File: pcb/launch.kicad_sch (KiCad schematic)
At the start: 250 parts, among them J1 Conn_ARM_SWD_TagConnect_TC2030, J6 SWD_TH, J7 AFC07-S20FCC-00, SW1 SKRPACE010, SW2 SKRPACE010, U1 RP2040, U24 W25Q16JVSSIQ, Y2 RH100-12.000-18-2030-TR

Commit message: hub reset handled by DC-DC power good switch to TLV62585P DC-DC for power good remove reset button - can just plug cable add buttons to ground SDA, SCL as hub bypass to allow programming
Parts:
- removed R35: 5.1 k, kicad_pcb:R_0402_1005Metric, symbol Device:R
- removed SW1: SKRPACE010, kicad_pcb:SW_SPST_PTS810, symbol Switch:SW_Push
- removed TP1, TP2: DNP, TestPoint:TestPoint_Loop_D1.80mm_Drill1.0mm_Beaded, symbol Connector:TestPoint
- added SW3, SW4: SKRPACE010, kicad_pcb:SW_SPST_PTS810, symbol Switch:SW_Push
- added TP1: Conn_01x03, Connector_PinHeader_2.54mm:PinHeader_1x03_P2.54mm_Vertical, symbol Connector_Generic:Conn_01x03
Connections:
- net RUN is gone; now on net +3V3: U1.26 (RUN)
- net GND: now also SW3.1, SW4.1, TP1.3 (Pin_3)
- net UC_SCL: now also SW4.2, TP1.1 (Pin_1)
- net UC_SDA: now also SW3.2, TP1.2 (Pin_2)
- net ~{RESET_USB}: no longer U1.31 (GPIO20)
- no-connect marks 3 -> 4
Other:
- sheet power ports: added PG; removed none
- note added: "hold SW3, SW4 while connecting power to use default USB hub configuration. This can be used to flash a blank or bricked board by USB DFU"
- note removed: "Reset"

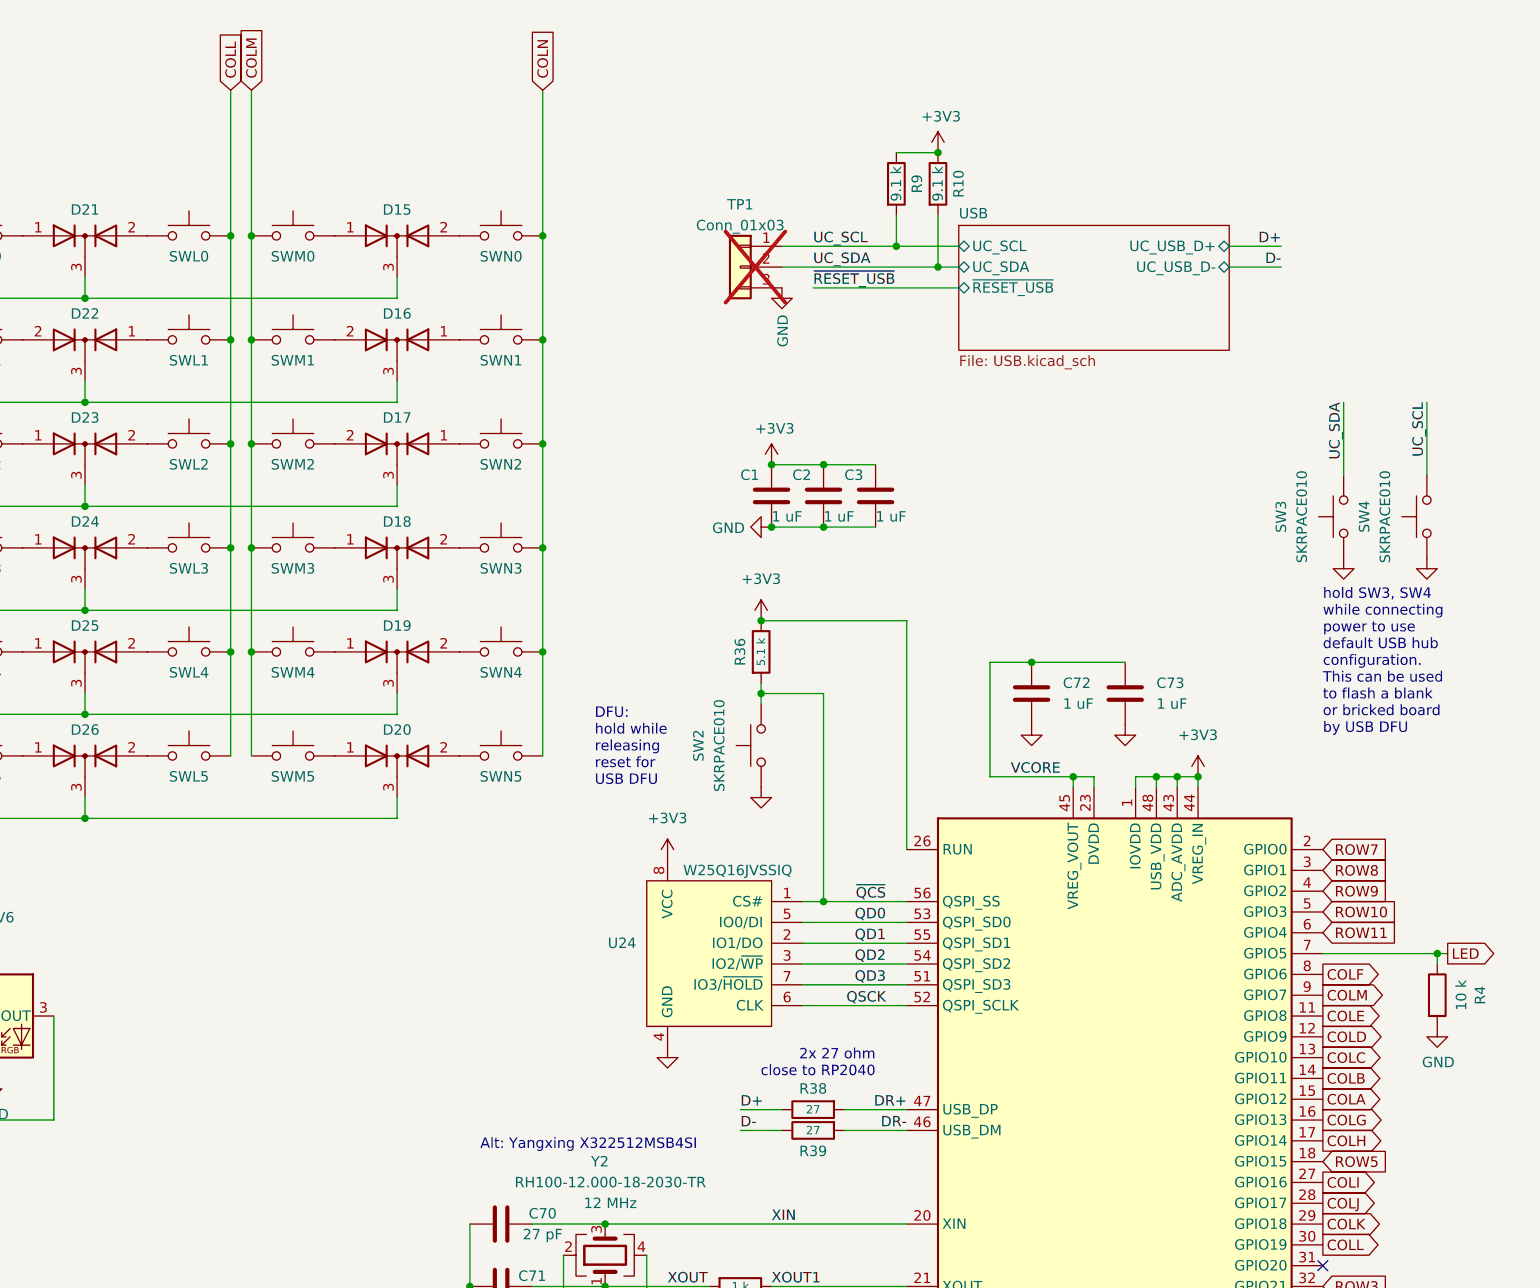
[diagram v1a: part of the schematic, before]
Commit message: single button for DFU boot also some ground stitching
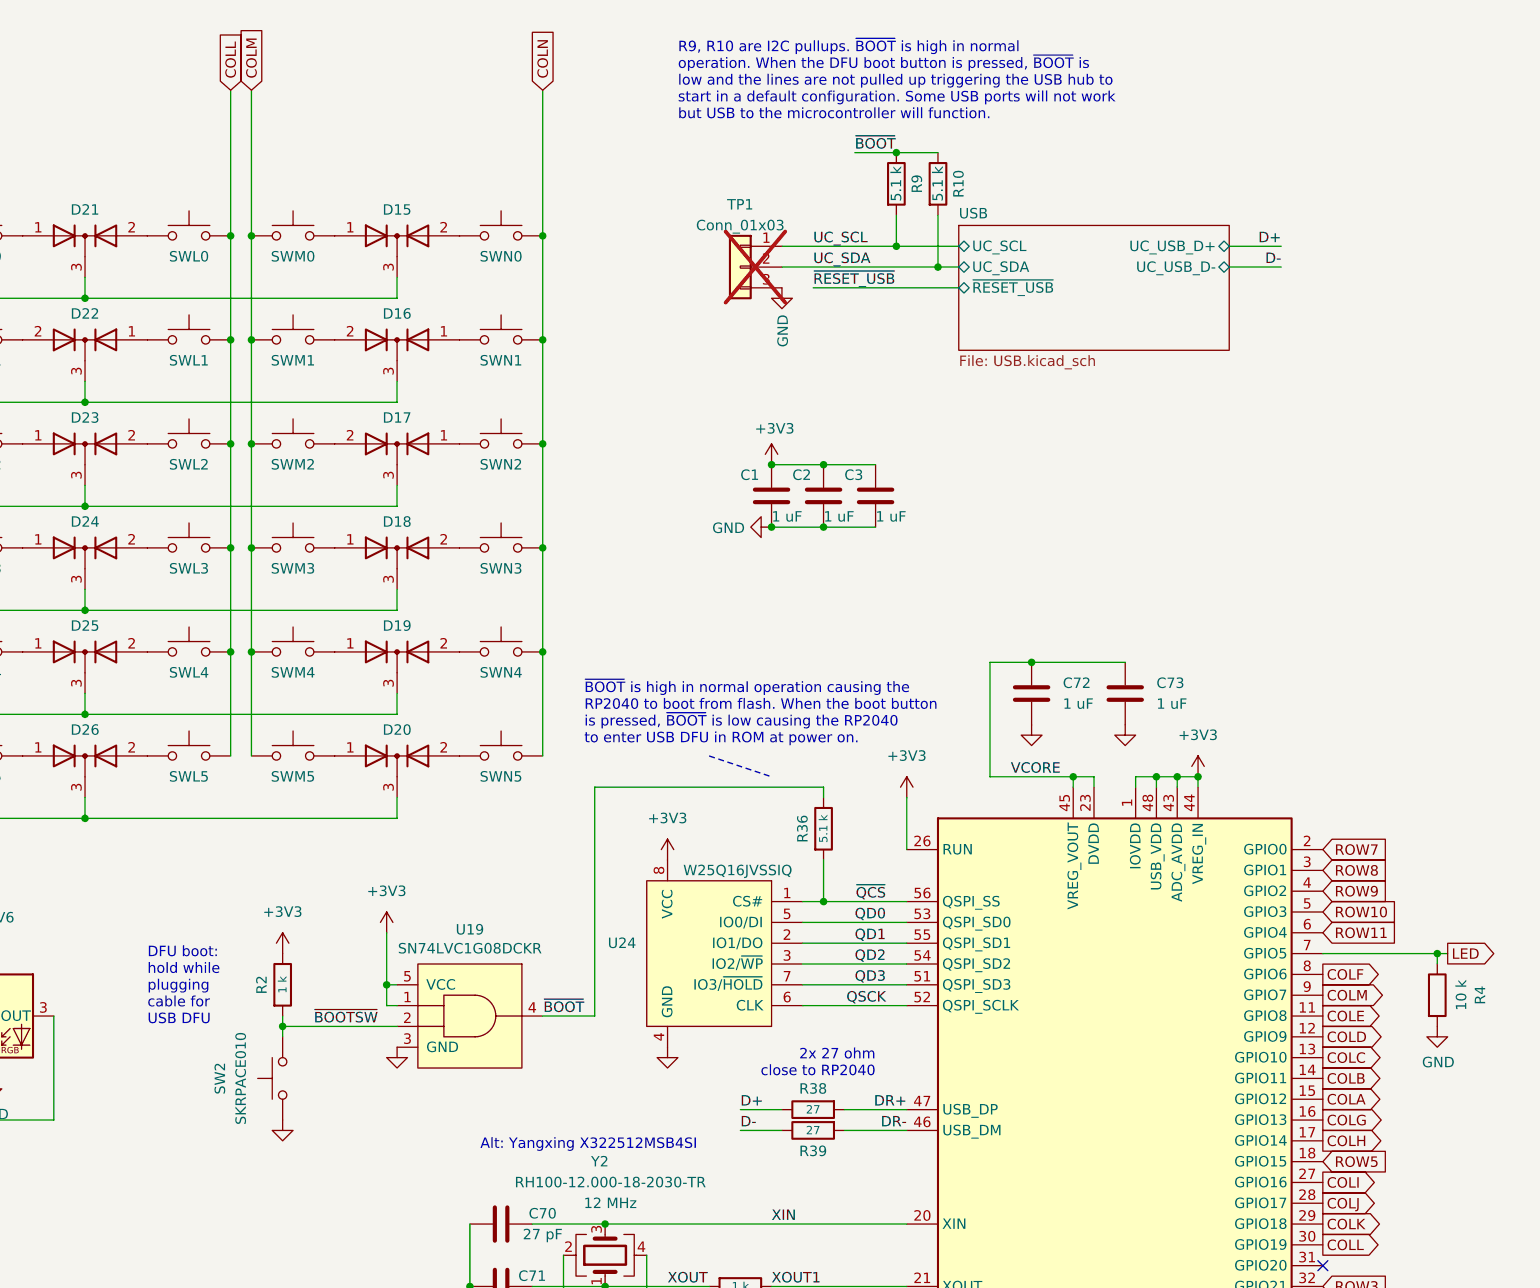
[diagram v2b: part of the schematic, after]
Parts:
- removed SW3, SW4: SKRPACE010, kicad_pcb:SW_SPST_PTS810, symbol Switch:SW_Push
- added R2: 1 k, kicad_pcb:R_0402_1005Metric, symbol Device:R
- added U19: SN74LVC1G08DCKR, Package_TO_SOT_SMD:SOT-353_SC-70-5, symbol launch:SN74LVC1G08DCKR
- R10, R9: value 9.1 k -> 5.1 k
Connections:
- net +3V3: now also R2.1, U19.1, U19.5 (VCC); no longer R10.1, R36.1, R9.1
- net GND: now also U19.3 (GND)
- net ~{QCS}: no longer SW2.2
- new net ~{BOOTSW}: R2.2, SW2.2, U19.2
- new net ~{BOOT}: R10.1, R36.1, R9.1, U19.4
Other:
- note added: "DFU boot: hold while plugging cable for USB DFU"
- note added: "R9, R10 are I2C pullups. ~{BOOT} is high in normal operation. When the DFU boot button is pressed, ~{BOOT} is low and the lines are not pulled up triggering the USB hub to start in a default configuration. Some USB ports will not work but USB to the microcontroller will function."
- note added: "~{BOOT} is high in normal operation causing the RP2040 to boot from flash. When the boot button is pressed, ~{BOOT} is low causing the RP2040 to enter USB DFU in ROM at power on."
- note removed: "DFU: hold while releasing reset for USB DFU"
- note removed: "hold SW3, SW4 while connecting power to use default USB hub configuration. This can be used to flash a blank or bricked board by USB DFU"
- moved on the sheet: R36, SW2

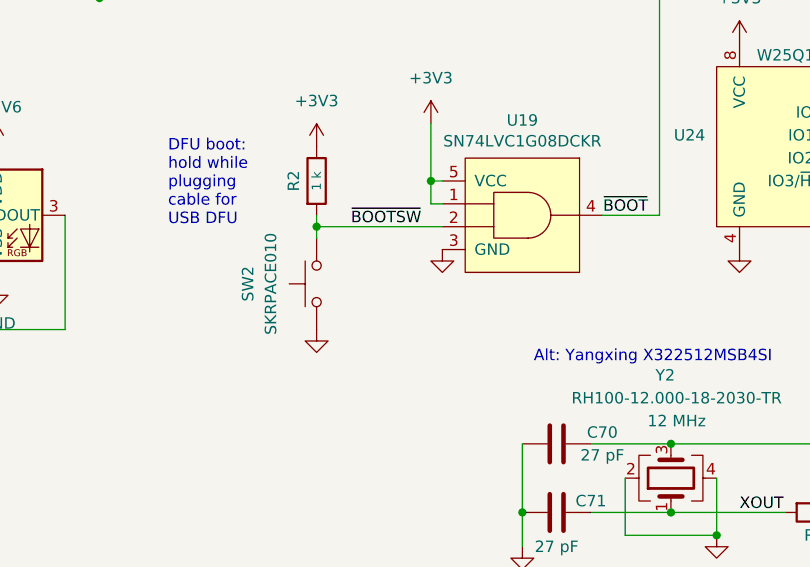
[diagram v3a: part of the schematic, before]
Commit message: change boot button to lower profile
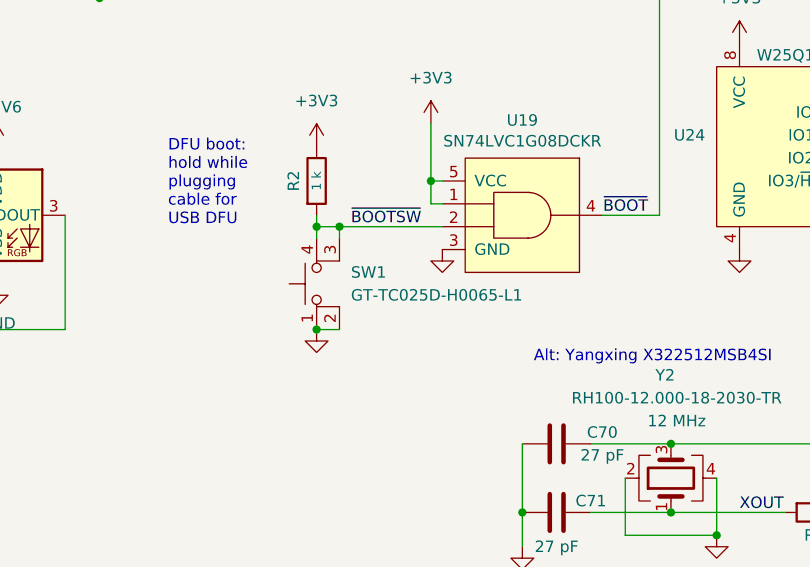
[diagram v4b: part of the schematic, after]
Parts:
- removed SW2: SKRPACE010, kicad_pcb:SW_SPST_PTS810, symbol Switch:SW_Push
- added SW1: GT-TC025D-H0065-L1, launch:GT-TC025D-H0065, symbol Switch:SW_MEC_5E
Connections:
- net GND: now also SW1.1, SW1.2
- net ~{BOOTSW}: now also SW1.3 (K), SW1.4 (A)
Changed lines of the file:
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@@
   (junction (at 298.45 166.37) (diameter 0) (color 0 0 0 0)
   )
+  (junction (at 261.62 134.62) (diameter 0) (color 0 0 0 0)
+  )
   (junction (at 138.43 76.2) (diameter 0) (color 0 0 0 0)
   )
@@
   (junction (at 158.75 58.42) (diameter 0) (color 0 0 0 0)
   )
+  (junction (at 259.08 146.05) (diameter 0) (color 0 0 0 0)
+  )
   (junction (at 255.27 76.2) (diameter 0) (color 0 0 0 0)
   )
@@
     (stroke (width 0) (type default))
   )
+  (wire (pts (xy 261.62 146.05) (xy 259.08 146.05))
+    (stroke (width 0) (type default))
+  )
   (wire (pts (xy 339.09 35.56) (xy 339.09 41.91))
     (stroke (width 0) (type default))
@@
     (stroke (width 0) (type default))
   )
+  (wire (pts (xy 261.62 134.62) (xy 273.05 134.62))
+    (stroke (width 0) (type default))
+  )
   (wire (pts (xy 138.43 76.2) (xy 138.43 88.9))
     (stroke (width 0) (type default))
@@
     (stroke (width 0) (type default))
   )
+  (wire (pts (xy 261.62 135.89) (xy 261.62 134.62))
+    (stroke (width 0) (type default))
+  )
   (wire (pts (xy 217.17 50.8) (xy 217.17 63.5))
     (stroke (width 0) (type default))
@@
     (stroke (width 0) (type default))
   )
-  (wire (pts (xy 259.08 134.62) (xy 273.05 134.62))
+  (wire (pts (xy 259.08 134.62) (xy 261.62 134.62))
     (stroke (width 0) (type default))
   )
@@
     )
   )
+  (symbol (lib_id "Switch:SW_MEC_5E") (at 261.62 140.97 90) (unit 1)
+    (in_bom yes) (on_board yes) (dnp no) (fields_autoplaced)
+    (property "Reference" "SW1" (at 262.89 139.7 90)
+      (effects (font (size 1.27 1.27)) (justify right))
+    )
+    (property "Value" "GT-TC025D-H0065-L1" (at 262.89 142.24 90)
+      (effects (font (size 1.27 1.27)) (justify right))
+    )
+    (property "Footprint" "launch:GT-TC025D-H0065" (at 254 140.97 0)
+      (effects (font (size 1.27 1.27)) hide)
+    )
+    (property "Datasheet" "https://datasheet.lcsc.com/lcsc/2009031909_G-Switch-GT-TC025D-H0065-L1_C778132.pdf" (at 254 140.97 0)
+      (effects (font (size 1.27 1.27)) hide)
+    )
+    (property "Manufacturer" "G-Switch" (at 261.62 140.97 0)
+      (effects (font (size 1.27 1.27)) hide)
+    )
+    (pin "1")
+    (pin "2")
+    (pin "3")
+    (pin "4")
+    (instances
+      (project "launch"
+        (path "/80c969df-cd39-4c4a-8336-5a366308cfd3"
+          (reference "SW1") (unit 1)
+        )
+      )
+    )
+  )
   (symbol (lib_id "Connector:Conn_ARM_SWD_TagConnect_TC2030") (at 295.91 189.23 0) (unit 1)
     (in_bom no) (on_board yes) (dnp no) (fields_autoplaced)
@@
         )
       )
-    )
-  )
-  (symbol (lib_id "Switch:SW_Push") (at 259.08 140.97 90) (unit 1)
-    (in_bom yes) (on_board yes) (dnp no) (fields_autoplaced)
-    (property "Reference" "SW2" (at 251.46 140.97 0)
-      (effects (font (size 1.27 1.27)))
-    )
-    (property "Value" "SKRPACE010" (at 254 140.97 0)
-      (effects (font (size 1.27 1.27)))
-    )
-    (property "Footprint" "kicad_pcb:SW_SPST_PTS810" (at 254 140.97 0)
-      (effects (font (size 1.27 1.27)) hide)
-    )
-    (property "Datasheet" "https://datasheet.lcsc.com/lcsc/1811051610_ALPSALPINE-SKRPACE010_C139797.pdf" (at 254 140.97 0)
-      (effects (font (size 1.27 1.27)) hide)
-    )
-    (property "Manufacturer" "Alps (generic equivalent OK)" (at 259.08 140.97 0)
-      (effects (font (size 1.27 1.27)) hide)
-    )
-    (pin "1")
-    (pin "2")
-    (instances
-      (project "launch"
-        (path "/80c969df-cd39-4c4a-8336-5a366308cfd3"
-          (reference "SW2") (unit 1)
-        )
-      )
-      (project "thelio-io"
-        (path "/e63e39d7-6ac0-4ffd-8aa3-1841a4541b55"
-          (reference "SW2") (unit 1)
-        )
-      )
